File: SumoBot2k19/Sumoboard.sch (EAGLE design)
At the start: 9 parts

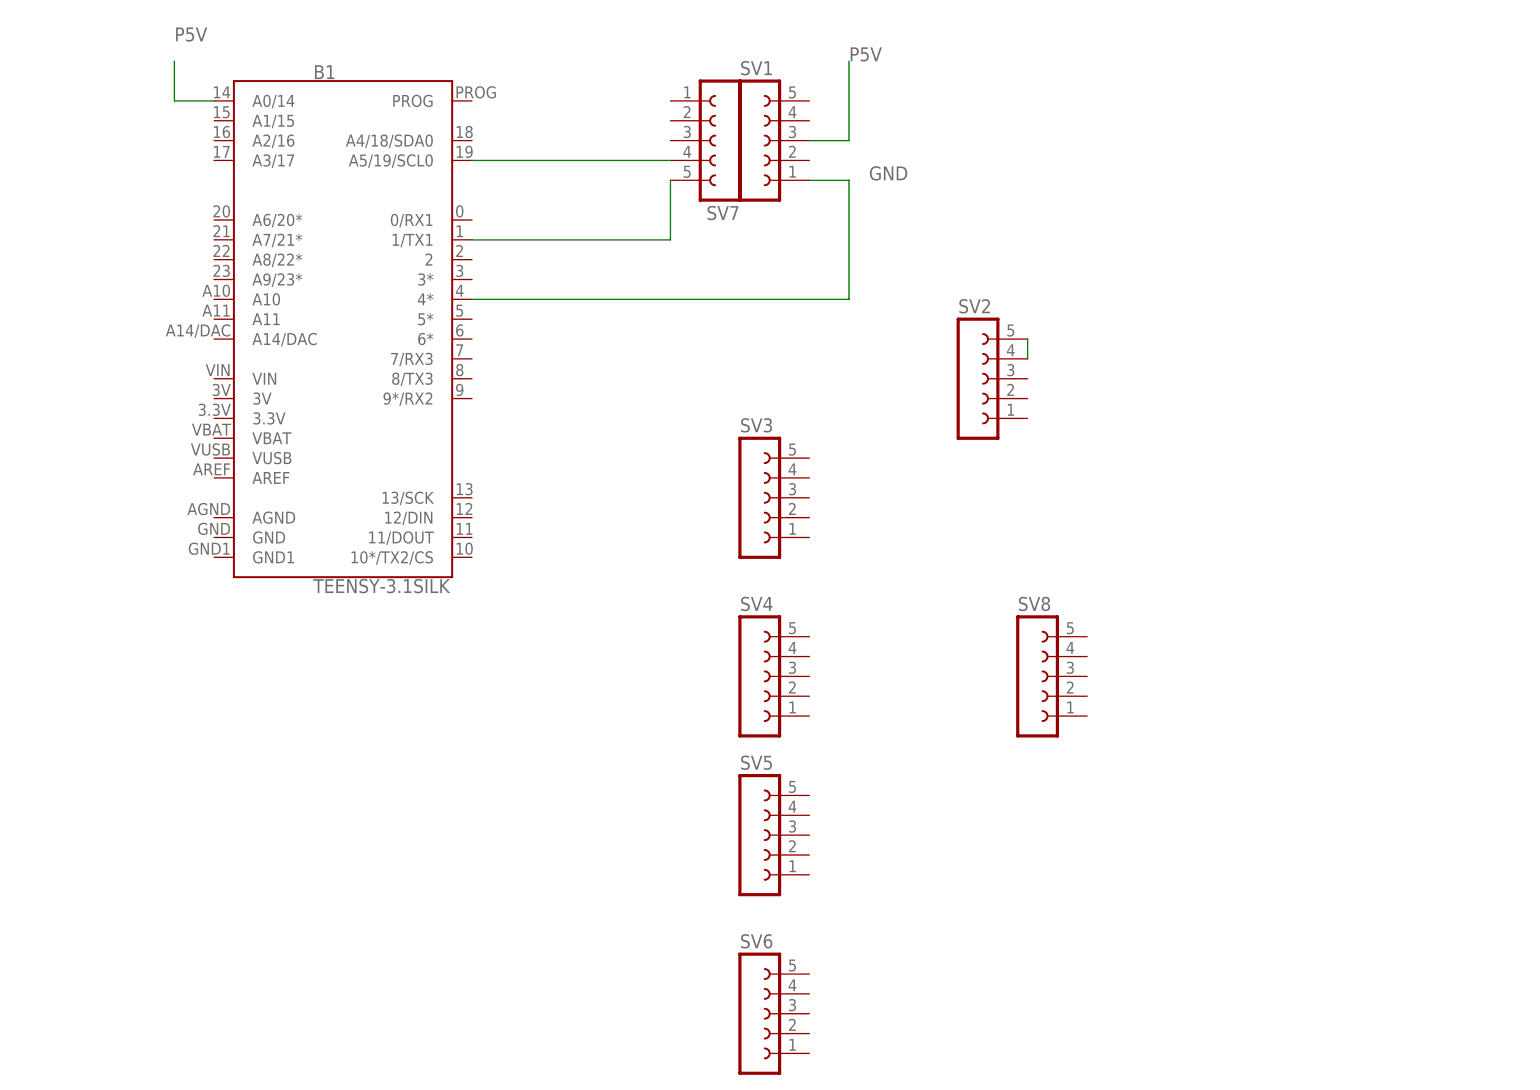
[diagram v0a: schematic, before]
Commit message: Substituted Winston's file
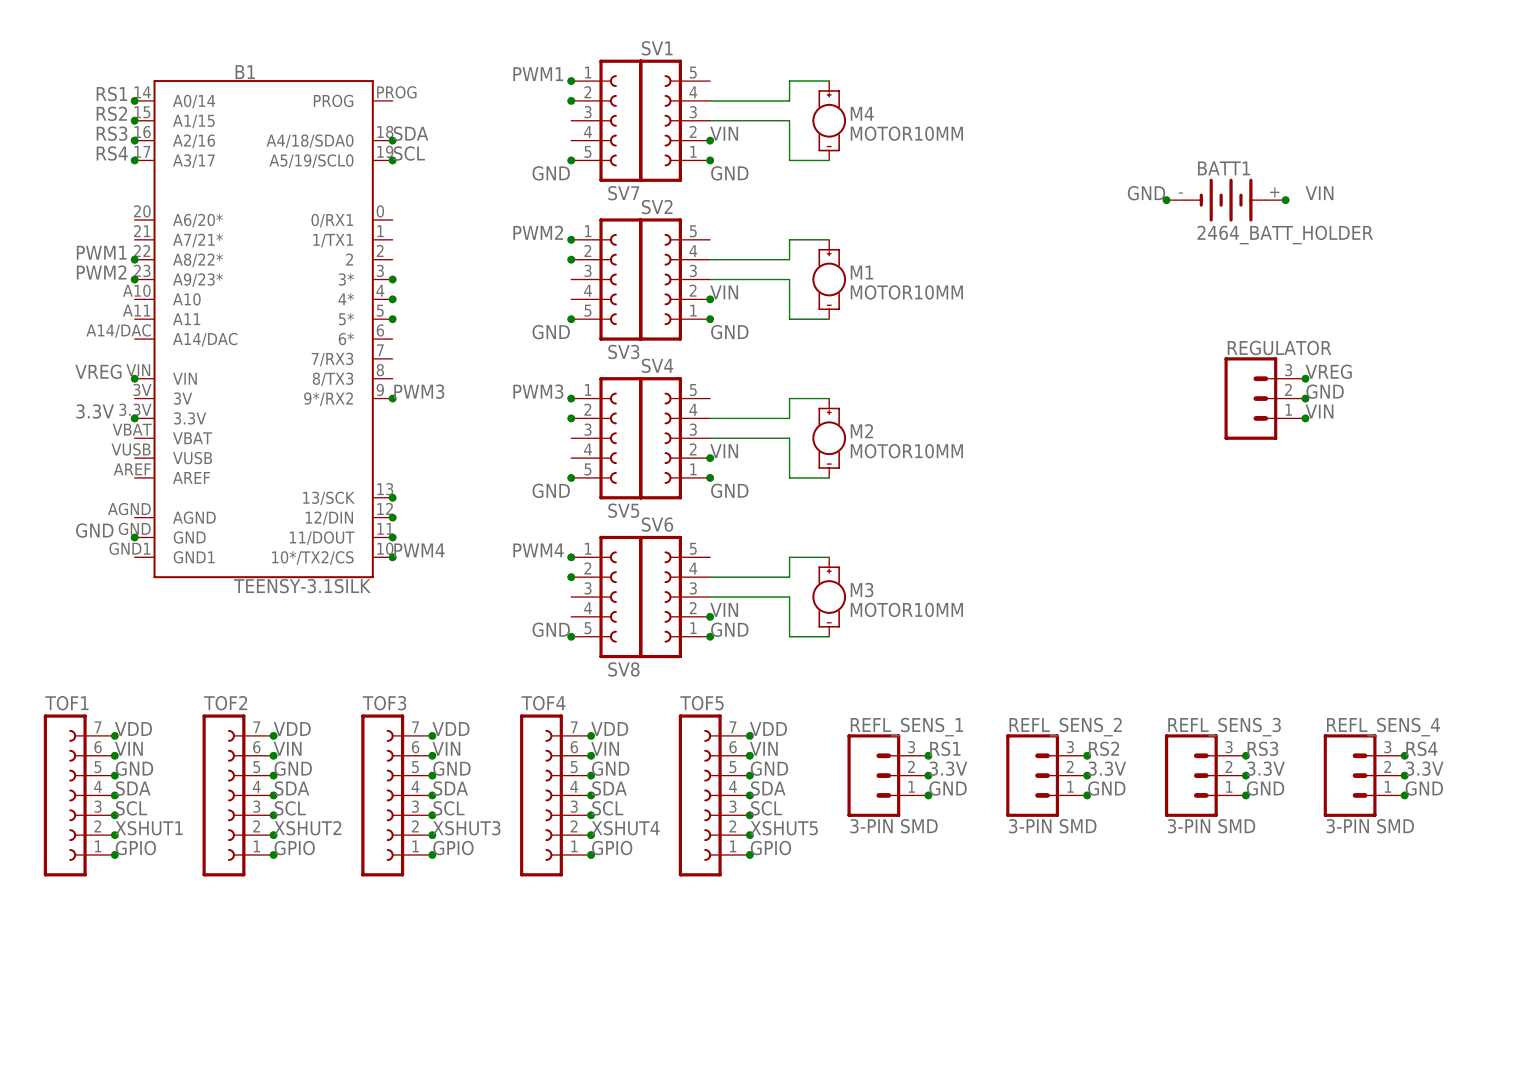
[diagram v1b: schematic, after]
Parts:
- added BATT1: 2464_BATT_HOLDER, DC_LOAD_AU:2464_BATT_HOLDER
- added M1, M2, M3, M4: MOTOR10MM, SparkFun-Electromechanical:MOTOR10MM
- added REFL_SENS_1, REFL_SENS_2, REFL_SENS_3, REFL_SENS_4: 3-PIN SMD, SparkFun-Connectors:CONN_03JST-SMD
- added REGULATOR: (no value), SparkFun-Connectors:CONN_03
- added TOF1, TOF2, TOF3, TOF4, TOF5: (no value), con-lsta:FE07-1
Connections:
- removed net N$3: B1.A5/19/SCL0, SV7.4
- removed net P5V: B1.A0/14, SV1.3
- new net 3.3V: B1.3.3V, REFL_SENS_1.2, REFL_SENS_2.2, REFL_SENS_3.2, REFL_SENS_4.2
- new net GPIO: TOF1.1, TOF2.1, TOF3.1, TOF4.1, TOF5.1
- new net N$12: B1.12/DIN
- new net N$13: B1.11/DOUT
- new net N$15: M1.+, SV2.4
- new net N$16: M1.-, SV2.3
- new net N$17: SV3.2
- new net N$19: M2.+, SV4.4
- new net N$20: M2.-, SV4.3
- new net N$21: SV5.2
- new net N$23: M3.+, SV6.4
- new net N$24: M3.-, SV6.3
- new net N$25: SV8.2
- new net N$6: B1.13/SCK
- new net N$7: SV7.2
- new net PWM1: B1.A8/22*, SV7.1
- new net PWM2: B1.A9/23*, SV3.1
- new net PWM3: B1.9*/RX2, SV5.1
- new net PWM4: B1.10*/TX2/CS, SV8.1
- new net RS1: B1.A0/14, REFL_SENS_1.3
- new net RS2: B1.3*, B1.A1/15, REFL_SENS_2.3
- new net RS3: B1.4*, B1.A2/16, REFL_SENS_3.3
- new net RS4: B1.5*, B1.A3/17, REFL_SENS_4.3
- new net SCL: B1.A5/19/SCL0, TOF1.3, TOF2.3, TOF3.3, TOF4.3, TOF5.3
- new net SDA: B1.A4/18/SDA0, TOF1.4, TOF2.4, TOF3.4, TOF4.4, TOF5.4
- new net VDD: TOF1.7, TOF2.7, TOF3.7, TOF4.7, TOF5.7
- new net VIN: BATT1.+, REGULATOR.1, SV1.2, SV2.2, SV4.2, SV6.2, TOF1.6, TOF2.6, TOF3.6, TOF4.6, TOF5.6
- new net VREG: B1.VIN, REGULATOR.3
- new net XSHUT1: TOF1.2
- new net XSHUT2: TOF2.2
- new net XSHUT3: TOF3.2
- new net XSHUT4: TOF4.2
- new net XSHUT5: TOF5.2
- net GND: now also B1.GND, BATT1.-, REFL_SENS_1.1, REFL_SENS_2.1, REFL_SENS_3.1, REFL_SENS_4.1, REGULATOR.2, SV2.1, SV3.5, SV4.1, SV5.5, SV6.1, SV7.5, SV8.5, TOF1.5, TOF2.5, TOF3.5, TOF4.5, TOF5.5; no longer B1.4*
- net N$1: now also M4.+, SV1.4; no longer B1.1/TX1, SV7.5
- net N$2: now also M4.-, SV1.3; no longer SV2.4, SV2.5
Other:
- moved on the sheet: B1, SV1, SV2, SV3, SV4, SV5, SV6, SV7, SV8

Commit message: added visual GND to schematic
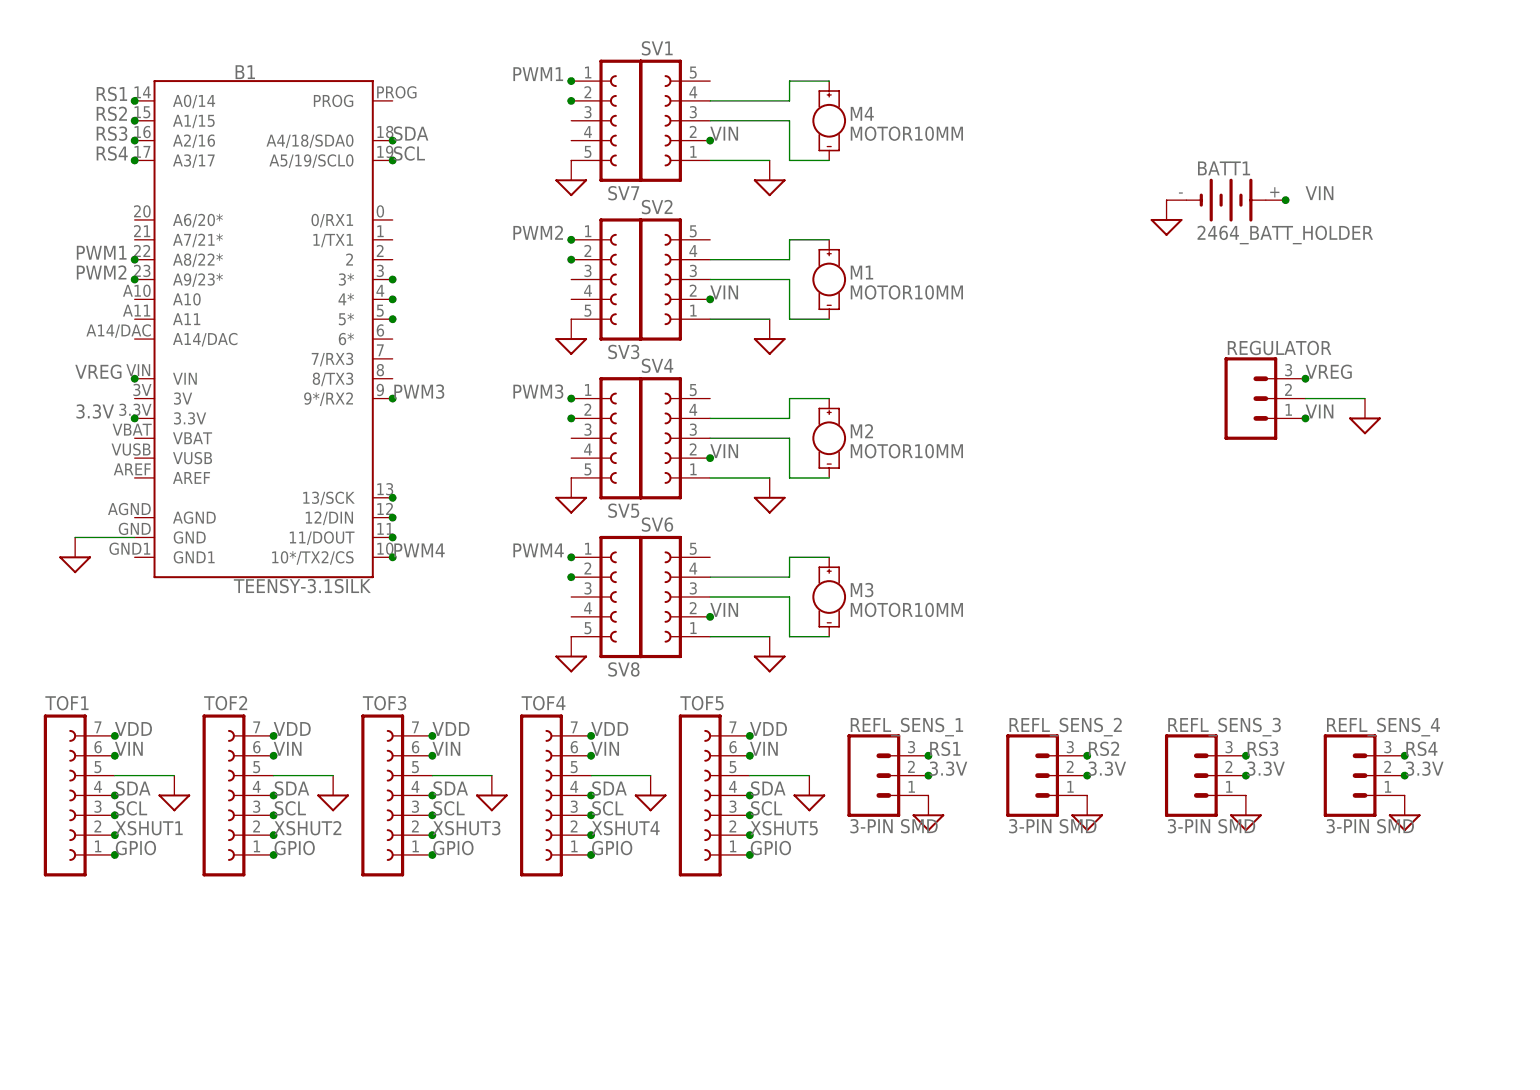
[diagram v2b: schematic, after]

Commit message: renamed and changed some pin numbers
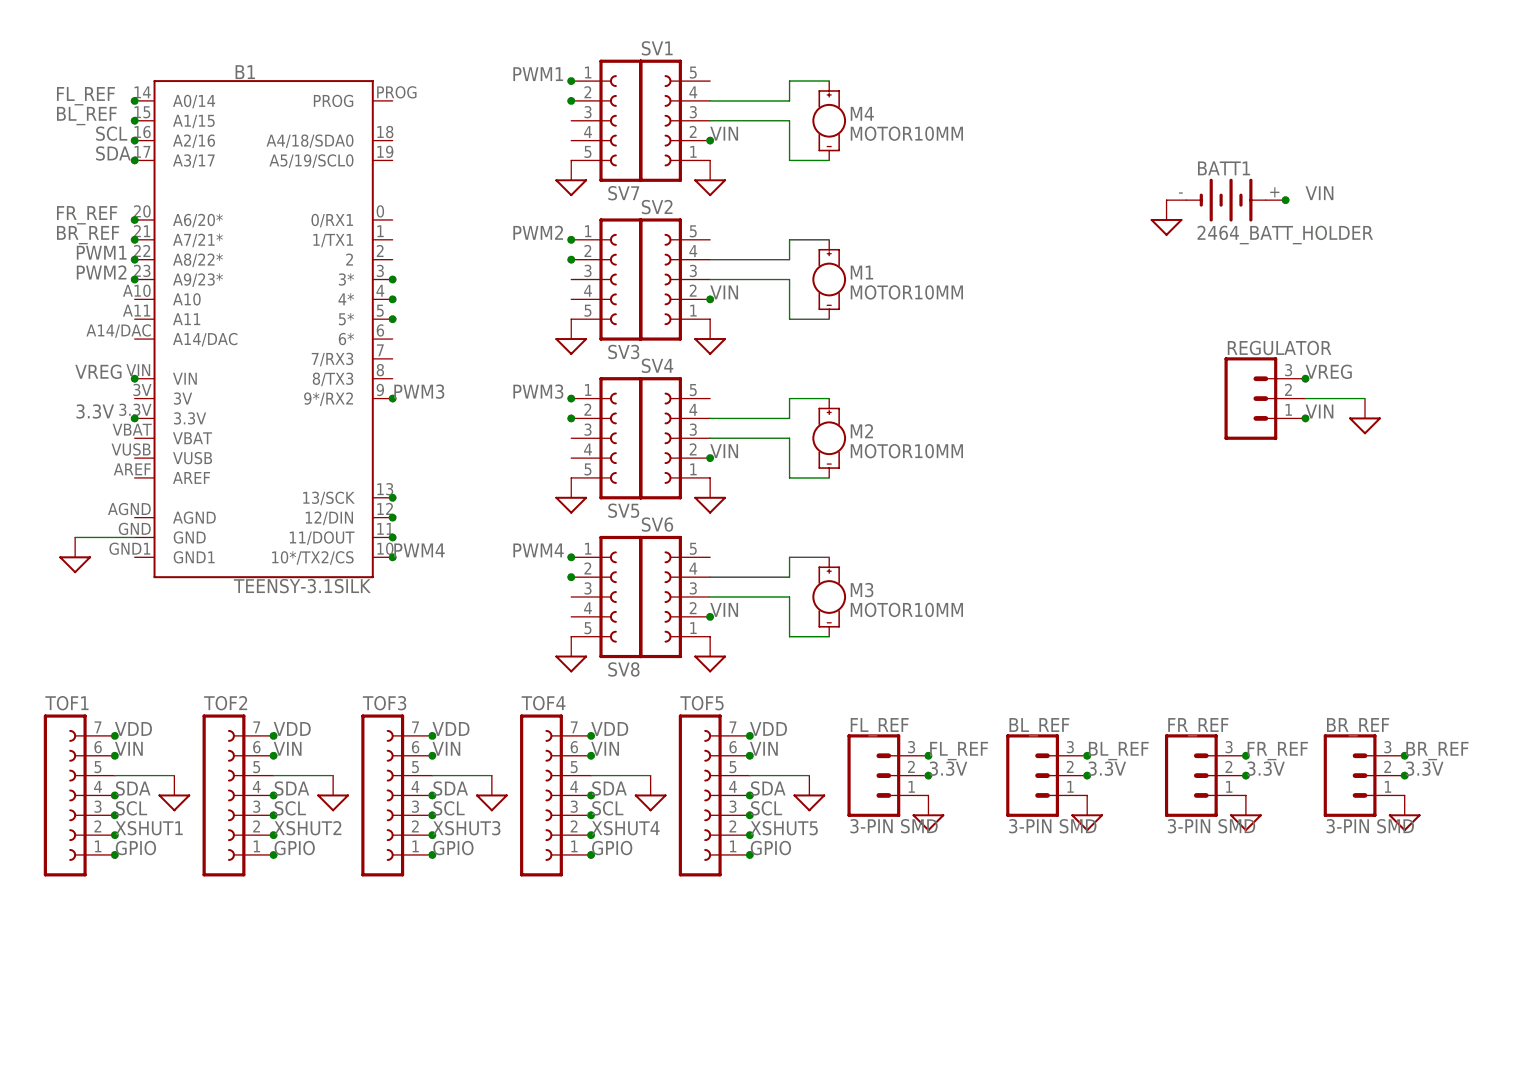
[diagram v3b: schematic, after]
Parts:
- renumbered REFL_SENS_1 to FL_REF, REFL_SENS_2 to BL_REF, REFL_SENS_3 to FR_REF, REFL_SENS_4 to BR_REF
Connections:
- net RS1 renamed FL_REF
- new net BL_REF: B1.A1/15, BL_REF.3
- new net BR_REF: B1.A7/21*, BR_REF.3
- new net FR_REF: B1.A6/20*, FR_REF.3
- net RS2: no longer B1.A1/15, BL_REF.3
- net RS3: no longer B1.A2/16, FR_REF.3
- net RS4: no longer B1.A3/17, BR_REF.3
- net SCL: now also B1.A2/16; no longer B1.A5/19/SCL0
- net SDA: now also B1.A3/17; no longer B1.A4/18/SDA0

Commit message: changed motor pins and added motor direction pins
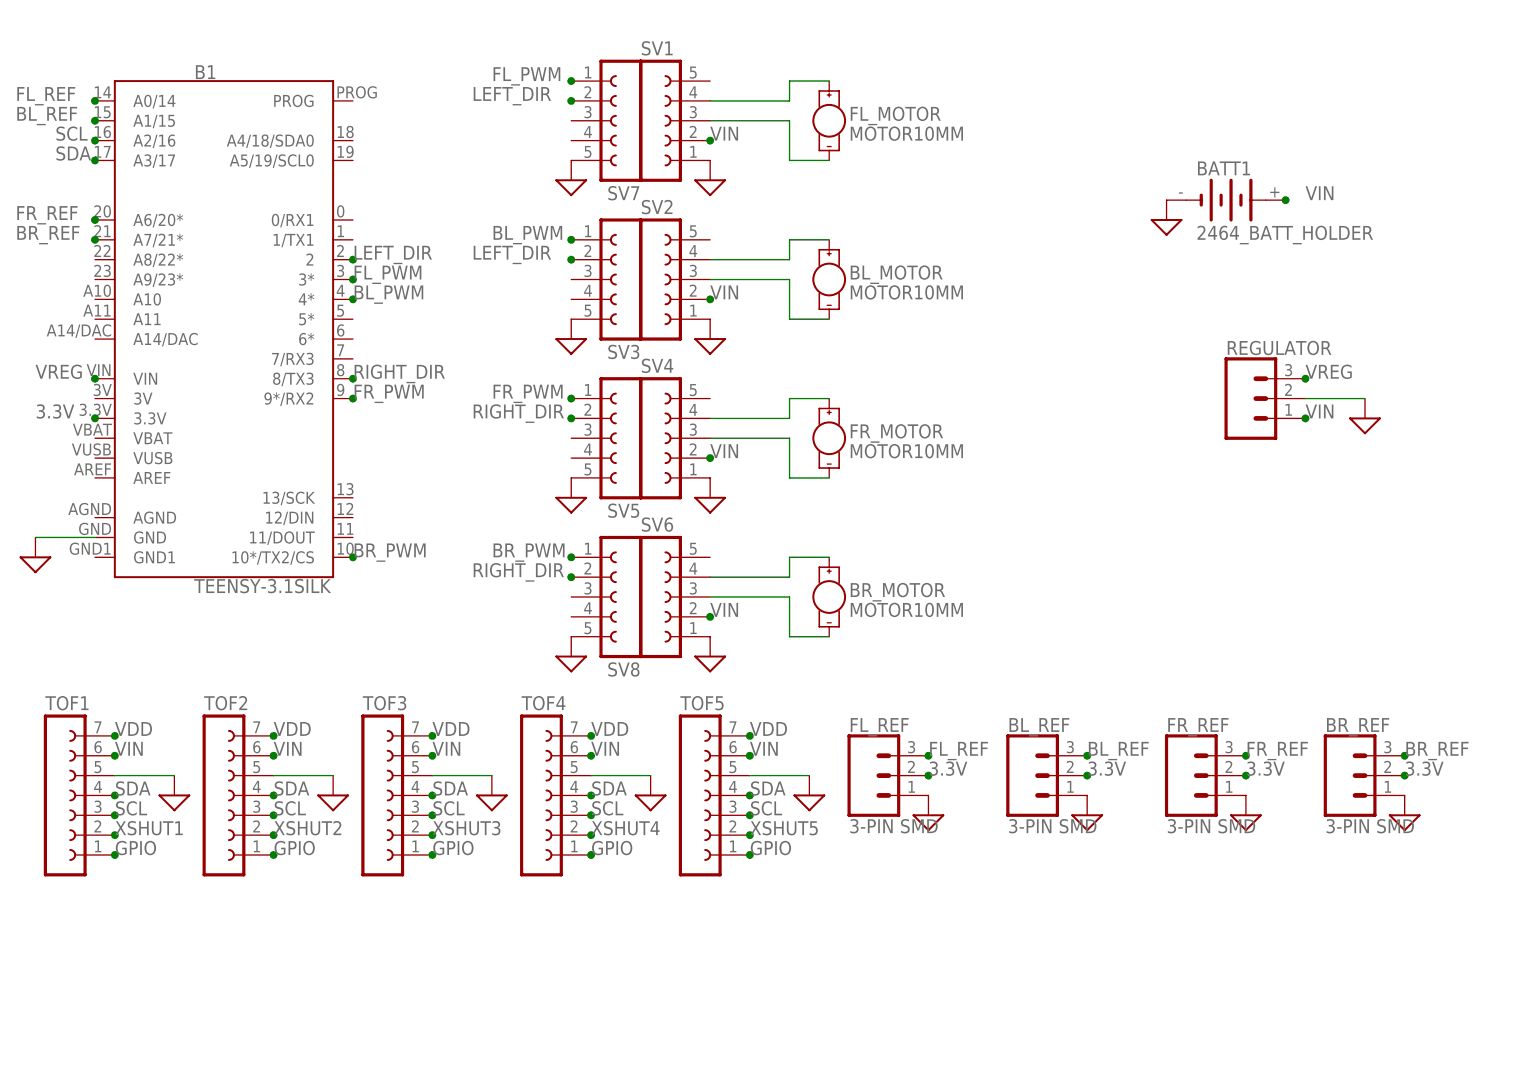
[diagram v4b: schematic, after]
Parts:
- renumbered M1 to BL_MOTOR, M2 to FR_MOTOR, M3 to BR_MOTOR, M4 to FL_MOTOR
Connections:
- net PWM3 renamed FR_PWM
- net PWM4 renamed BR_PWM
- removed net N$12: B1.12/DIN
- removed net N$13: B1.11/DOUT
- removed net N$17: SV3.2
- removed net N$21: SV5.2
- removed net N$25: SV8.2
- removed net N$6: B1.13/SCK
- removed net N$7: SV7.2
- removed net PWM1: B1.A8/22*, SV7.1
- removed net PWM2: B1.A9/23*, SV3.1
- removed net RS2: B1.3*
- removed net RS3: B1.4*
- removed net RS4: B1.5*
- new net BL_PWM: B1.4*, SV3.1
- new net FL_PWM: B1.3*, SV7.1
- new net LEFT_DIR: B1.2, SV3.2, SV7.2
- new net RIGHT_DIR: B1.8/TX3, SV5.2, SV8.2
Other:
- moved on the sheet: B1
